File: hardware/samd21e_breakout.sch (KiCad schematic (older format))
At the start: 12 parts, among them J1 USB_B_Micro, J2 Conn_01x26_Male, J3 Conn_01x08_Male, SW1 SW_Push, U1 AP2112K-3.3, U2 ATSAMD21E18A, Y1 32.768 kHz

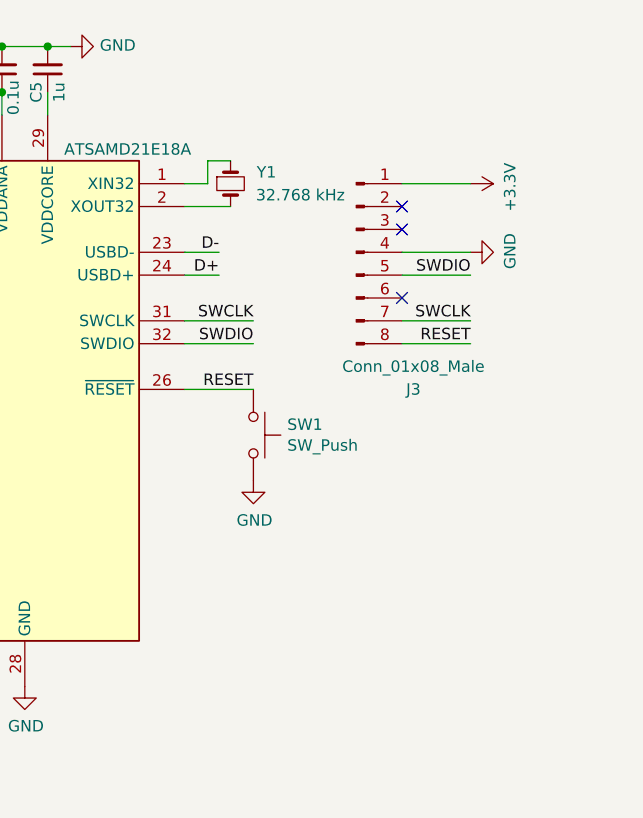
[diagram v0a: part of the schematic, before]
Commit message: added load capacitors to schematic and pcb
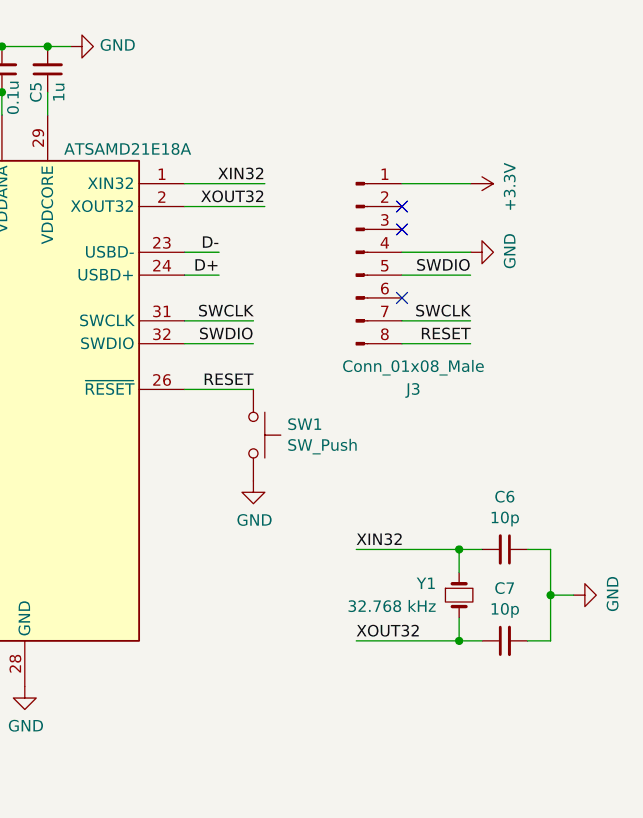
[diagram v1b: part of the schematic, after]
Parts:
- added C6, C7: 10p, samd21e_breakout:C_0603_NoSilk, symbol Device:C_Small
- C1, C2, C3, C4, C5: footprint minimal_samd21_breakout:C_0603_NoSilk -> samd21e_breakout:C_0603_NoSilk
- J1: footprint minimal_samd21_breakout:Molex-105017-0001 -> samd21e_breakout:Molex-105017-0001
- J2: footprint minimal_samd21_breakout:PinHeader_2x13_Breadboard_Spaced -> samd21e_breakout:PinHeader_2x13_Breadboard_Spaced
- J3: footprint minimal_samd21_breakout:SOIC_clipProgSmall -> samd21e_breakout:SOIC_clipProgSmall
- SW1: footprint minimal_samd21_breakout:SW_Push_Alps_SKRK_NoSilk -> samd21e_breakout:SW_Push_Alps_SKRK_NoSilk
- U1: footprint minimal_samd21_breakout:SOT-23-5_NoSilk -> samd21e_breakout:SOT-23-5_NoSilk
- U2: footprint minimal_samd21_breakout:TQFP-32_NoSilk -> samd21e_breakout:TQFP-32_NoSilk
- Y1: footprint minimal_samd21_breakout:CM7V-T1A -> samd21e_breakout:CM7V-T1A
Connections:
- net GND: now also C6.1, C7.2
- net XIN32: now reaches U2.1 (XIN32), Y1.1
- net XIN32: now also C6.2
- net XOUT32: now reaches U2.2 (XOUT32), Y1.2
- net XOUT32: now also C7.1
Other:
- moved on the sheet: Y1
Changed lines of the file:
@@
 F 0 "U2" H 3450 3250 50  0000 C CNN
 F 1 "ATSAMD21E18A" H 4550 3250 50  0000 C CNN
-F 2 "minimal_samd21_breakout:TQFP-32_NoSilk" H 5100 2900 50  0001 C CNN
+F 2 "samd21e_breakout:TQFP-32_NoSilk" H 5100 2900 50  0001 C CNN
 F 3 "" V 4000 3050 50  0001 C CNN
 	1    4000 2150
@@
 F 0 "C5" V 4250 800 50  0000 C CNN
 F 1 "1u" V 4150 800 50  0000 C CNN
-F 2 "minimal_samd21_breakout:C_0603_NoSilk" H 4200 700 50  0001 C CNN
+F 2 "samd21e_breakout:C_0603_NoSilk" H 4200 700 50  0001 C CNN
 F 3 "~" H 4200 700 50  0001 C CNN
 	1    4200 700
@@
 F 0 "C3" V 3850 850 50  0000 R CNN
 F 1 "0.1u" V 3750 900 50  0000 R CNN
-F 2 "minimal_samd21_breakout:C_0603_NoSilk" H 3800 700 50  0001 C CNN
+F 2 "samd21e_breakout:C_0603_NoSilk" H 3800 700 50  0001 C CNN
 F 3 "~" H 3800 700 50  0001 C CNN
 	1    3800 700
@@
 F 0 "J1" H 807 1467 50  0000 C CNN
 F 1 "USB_B_Micro" H 807 1376 50  0000 C CNN
-F 2 "minimal_samd21_breakout:Molex-105017-0001" H 900 950 50  0001 C CNN
+F 2 "samd21e_breakout:Molex-105017-0001" H 900 950 50  0001 C CNN
 F 3 "~" H 900 950 50  0001 C CNN
 	1    750  1000
@@
 F 0 "C1" H 1258 954 50  0000 R CNN
 F 1 "10u" H 1258 1045 50  0000 R CNN
-F 2 "minimal_samd21_breakout:C_0603_NoSilk" H 1350 1000 50  0001 C CNN
+F 2 "samd21e_breakout:C_0603_NoSilk" H 1350 1000 50  0001 C CNN
 F 3 "~" H 1350 1000 50  0001 C CNN
 	1    1350 1000
@@
 F 0 "U1" H 1950 1242 50  0000 C CNN
 F 1 "AP2112K-3.3" H 1950 1151 50  0000 C CNN
-F 2 "minimal_samd21_breakout:SOT-23-5_NoSilk" H 1950 1225 50  0001 C CNN
+F 2 "samd21e_breakout:SOT-23-5_NoSilk" H 1950 1225 50  0001 C CNN
 F 3 "https://www.diodes.com/assets/Datasheets/AP2112.pdf" H 1950 1000 50  0001 C CNN
 	1    1950 900
@@
 F 0 "C2" H 2258 954 50  0000 R CNN
 F 1 "10u" H 2258 1045 50  0000 R CNN
-F 2 "minimal_samd21_breakout:C_0603_NoSilk" H 2350 1000 50  0001 C CNN
+F 2 "samd21e_breakout:C_0603_NoSilk" H 2350 1000 50  0001 C CNN
 F 3 "~" H 2350 1000 50  0001 C CNN
 	1    2350 1000
@@
 L Device:Crystal_Small Y1
 U 1 1 5E95328C
-P 5000 1200
-F 0 "Y1" V 4950 1400 50  0000 R CNN
-F 1 "32.768 kHz" V 5050 1700 50  0000 R CNN
-F 2 "minimal_samd21_breakout:CM7V-T1A" H 5000 1200 50  0001 C CNN
-F 3 "~" H 5000 1200 50  0001 C CNN
-	1    5000 1200
+P 6000 3000
+F 0 "Y1" V 5950 2900 50  0000 R CNN
+F 1 "32.768 kHz" V 6050 2900 50  0000 R CNN
+F 2 "samd21e_breakout:CM7V-T1A" H 6000 3000 50  0001 C CNN
+F 3 "~" H 6000 3000 50  0001 C CNN
+	1    6000 3000
 	0    1    1    0
 $EndComp
@@
 F 0 "J3" H 5800 900 50  0000 C CNN
 F 1 "Conn_01x08_Male" H 5800 1000 50  0000 C CNN
-F 2 "minimal_samd21_breakout:SOIC_clipProgSmall" H 5550 1500 50  0001 C CNN
+F 2 "samd21e_breakout:SOIC_clipProgSmall" H 5550 1500 50  0001 C CNN
 F 3 "~" H 5550 1500 50  0001 C CNN
 	1    5550 1500
@@
 F 0 "C4" V 4050 850 50  0000 R CNN
 F 1 "0.1u" V 3950 900 50  0000 R CNN
-F 2 "minimal_samd21_breakout:C_0603_NoSilk" H 4000 700 50  0001 C CNN
+F 2 "samd21e_breakout:C_0603_NoSilk" H 4000 700 50  0001 C CNN
 F 3 "~" H 4000 700 50  0001 C CNN
 	1    4000 700
@@
 Connection ~ 4000 600
 Wire Wire Line
-	4800 1300 5000 1300
-Wire Wire Line
-	5000 1100 4900 1100
-Wire Wire Line
-	4900 1100 4900 1200
-Wire Wire Line
-	4900 1200 4800 1200
-Wire Wire Line
 	4000 600  4200 600
 Connection ~ 4200 600
@@
 F 0 "J2" H 1658 4631 50  0000 C CNN
 F 1 "Conn_01x26_Male" H 1658 4540 50  0000 C CNN
-F 2 "minimal_samd21_breakout:PinHeader_2x13_Breadboard_Spaced" H 1550 3250 50  0001 C CNN
+F 2 "samd21e_breakout:PinHeader_2x13_Breadboard_Spaced" H 1550 3250 50  0001 C CNN
 F 3 "~" H 1550 3250 50  0001 C CNN
 	1    1550 3250
@@
 F 0 "SW1" V 5054 2448 50  0000 L CNN
 F 1 "SW_Push" V 5145 2448 50  0000 L CNN
-F 2 "minimal_samd21_breakout:SW_Push_Alps_SKRK_NoSilk" H 5100 2500 50  0001 C CNN
+F 2 "samd21e_breakout:SW_Push_Alps_SKRK_NoSilk" H 5100 2500 50  0001 C CNN
 F 3 "~" H 5100 2500 50  0001 C CNN
 	1    5100 2300
@@
 	1    0    0    -1
 $EndComp
+$Comp
+L Device:C_Small C6
+U 1 1 5EE41B8D
+P 6200 2800
+F 0 "C6" V 5971 2800 50  0000 C CNN
+F 1 "10p" V 6062 2800 50  0000 C CNN
+F 2 "samd21e_breakout:C_0603_NoSilk" H 6200 2800 50  0001 C CNN
+F 3 "~" H 6200 2800 50  0001 C CNN
+	1    6200 2800
+	0    1    1    0
+$EndComp
+Wire Wire Line
+	6000 2900 6000 2800
+Wire Wire Line
+	6000 2800 6100 2800
+Wire Wire Line
+	6000 3100 6000 3200
+Wire Wire Line
+	6000 3200 6100 3200
+Connection ~ 6000 3200
+Connection ~ 6000 2800
+Text Label 5150 1200 2    50   ~ 0
+XIN32
+Text Label 5150 1300 2    50   ~ 0
+XOUT32
+Wire Wire Line
+	4800 1200 5150 1200
+Wire Wire Line
+	4800 1300 5150 1300
+Text Label 5550 2800 0    50   ~ 0
+XIN32
+Text Label 5550 3200 0    50   ~ 0
+XOUT32
+Wire Wire Line
+	5550 2800 6000 2800
+Wire Wire Line
+	5550 3200 6000 3200
+$Comp
+L Device:C_Small C7
+U 1 1 5EE68034
+P 6200 3200
+F 0 "C7" V 6429 3200 50  0000 C CNN
+F 1 "10p" V 6338 3200 50  0000 C CNN
+F 2 "samd21e_breakout:C_0603_NoSilk" H 6200 3200 50  0001 C CNN
+F 3 "~" H 6200 3200 50  0001 C CNN
+	1    6200 3200
+	0    -1   -1   0
+$EndComp
+Wire Wire Line
+	6300 2800 6400 2800
+Wire Wire Line
+	6400 2800 6400 3000
+Wire Wire Line
+	6400 3200 6300 3200
+Wire Wire Line
+	6400 3000 6500 3000
+Connection ~ 6400 3000
+Wire Wire Line
+	6400 3000 6400 3200
+$Comp
+L power:GND #PWR0106
+U 1 1 5EE7625D
+P 6500 3000
+F 0 "#PWR0106" H 6500 2750 50  0001 C CNN
+F 1 "GND" H 6505 2827 50  0000 C CNN
+F 2 "" H 6500 3000 50  0001 C CNN
+F 3 "" H 6500 3000 50  0001 C CNN
+	1    6500 3000
+	0    -1   -1   0
+$EndComp
 $EndSCHEMATC
